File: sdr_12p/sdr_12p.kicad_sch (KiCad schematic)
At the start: 13 parts, among them J1 Rx, J10 ADAU1467_GPIOS, J11 ADAU1467_AUX_ADCS, J2 Tx, J3 6V, J4 2V, J5 4V, J6 Microcontroller, J7 USBi, J8 I2S2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

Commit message: changed project names
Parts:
- removed J4: 2V, symbol Connector:Screw_Terminal_01x02
- removed TR3, TR4: ADT4-6T, RF_Mini-Circuits:Mini-Circuits_CD637_H5.23mm, symbol Transformer:ADT4-6T
- added TR1, TR2: ADT1-1WT, RF_Mini-Circuits:Mini-Circuits_CD542_H2.84mm, symbol Transformer:ADT1-1WT

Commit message: basic arrangement of blocks
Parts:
- removed J5: 4V, symbol Connector:Screw_Terminal_01x02
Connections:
- net 6V renamed 6 - 20V
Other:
- sheet TRIPLE_ADAU1979 renamed TRIPLE_ADAU1978
- added sheet Coarse_VFO (coarse_vfo.kicad_sch)
- added sheet Microcontroller (microcontroller.kicad_sch)
- added sheet Power_Mgmt (power_mgmt.kicad_sch)
- sheet TRIPLE_ADAU1978: file triple_adau1979.kicad_sch -> triple_adau1978.kicad_sch
- title: HF Software Defined Radio with 32 Phase Polyphase Mixer -> HF Software Defined Radio with Polyphase Mixer (12 Phase)
- moved on the sheet: J10, J11, J3, J6, J7, J8, J9

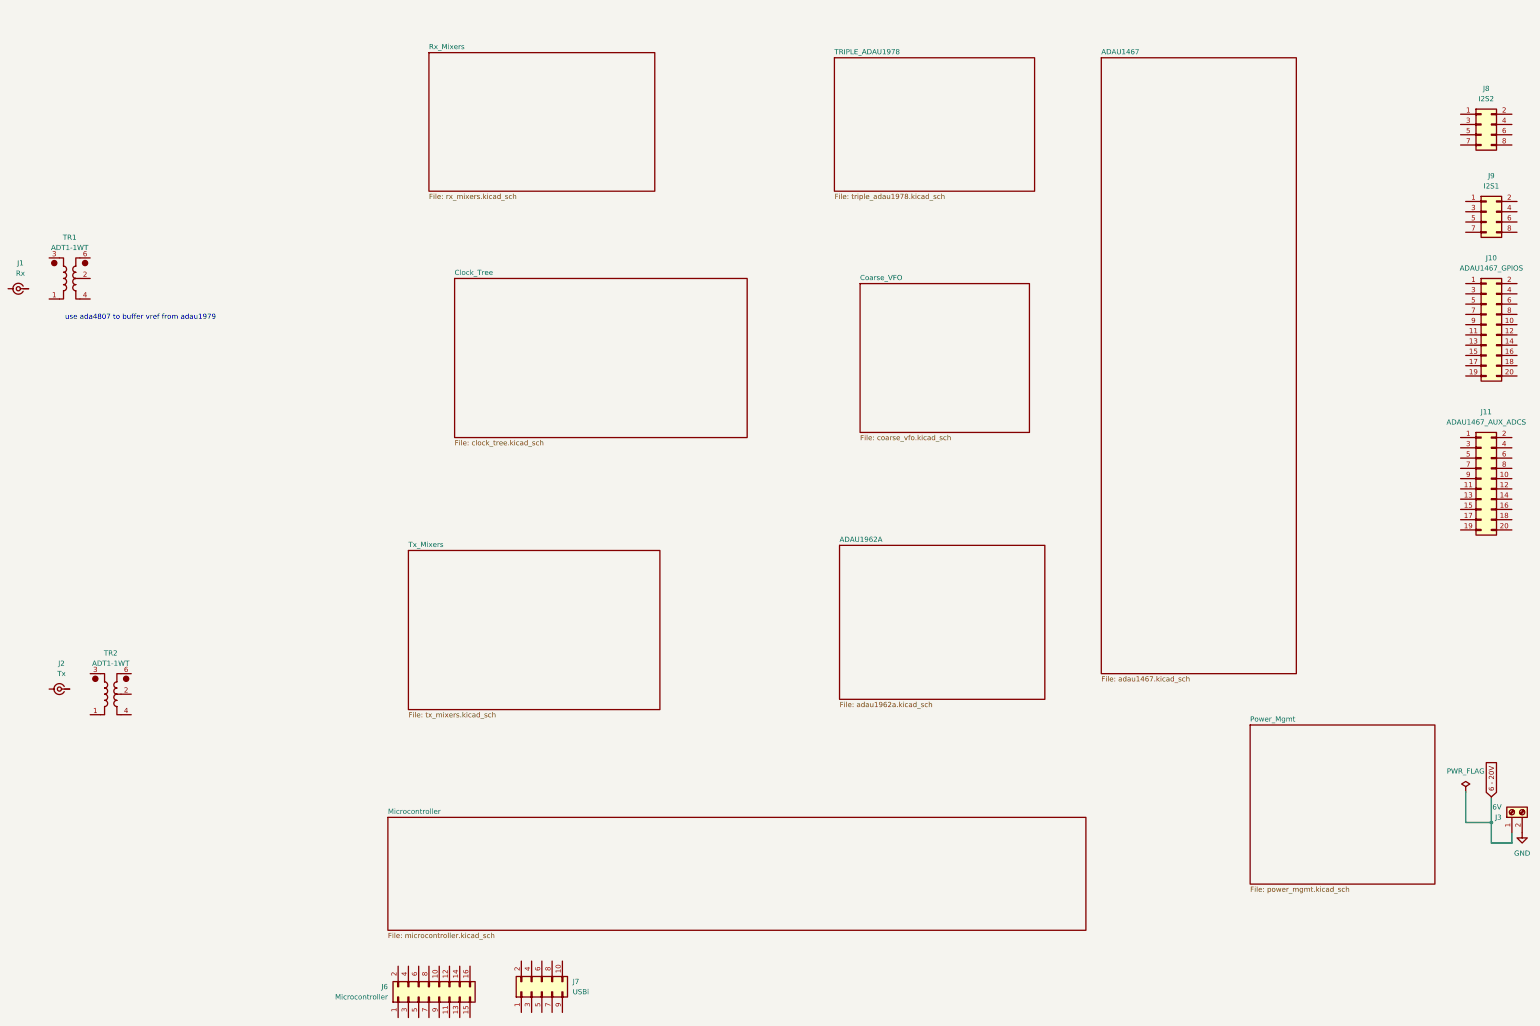
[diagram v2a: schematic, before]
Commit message: added rx switches
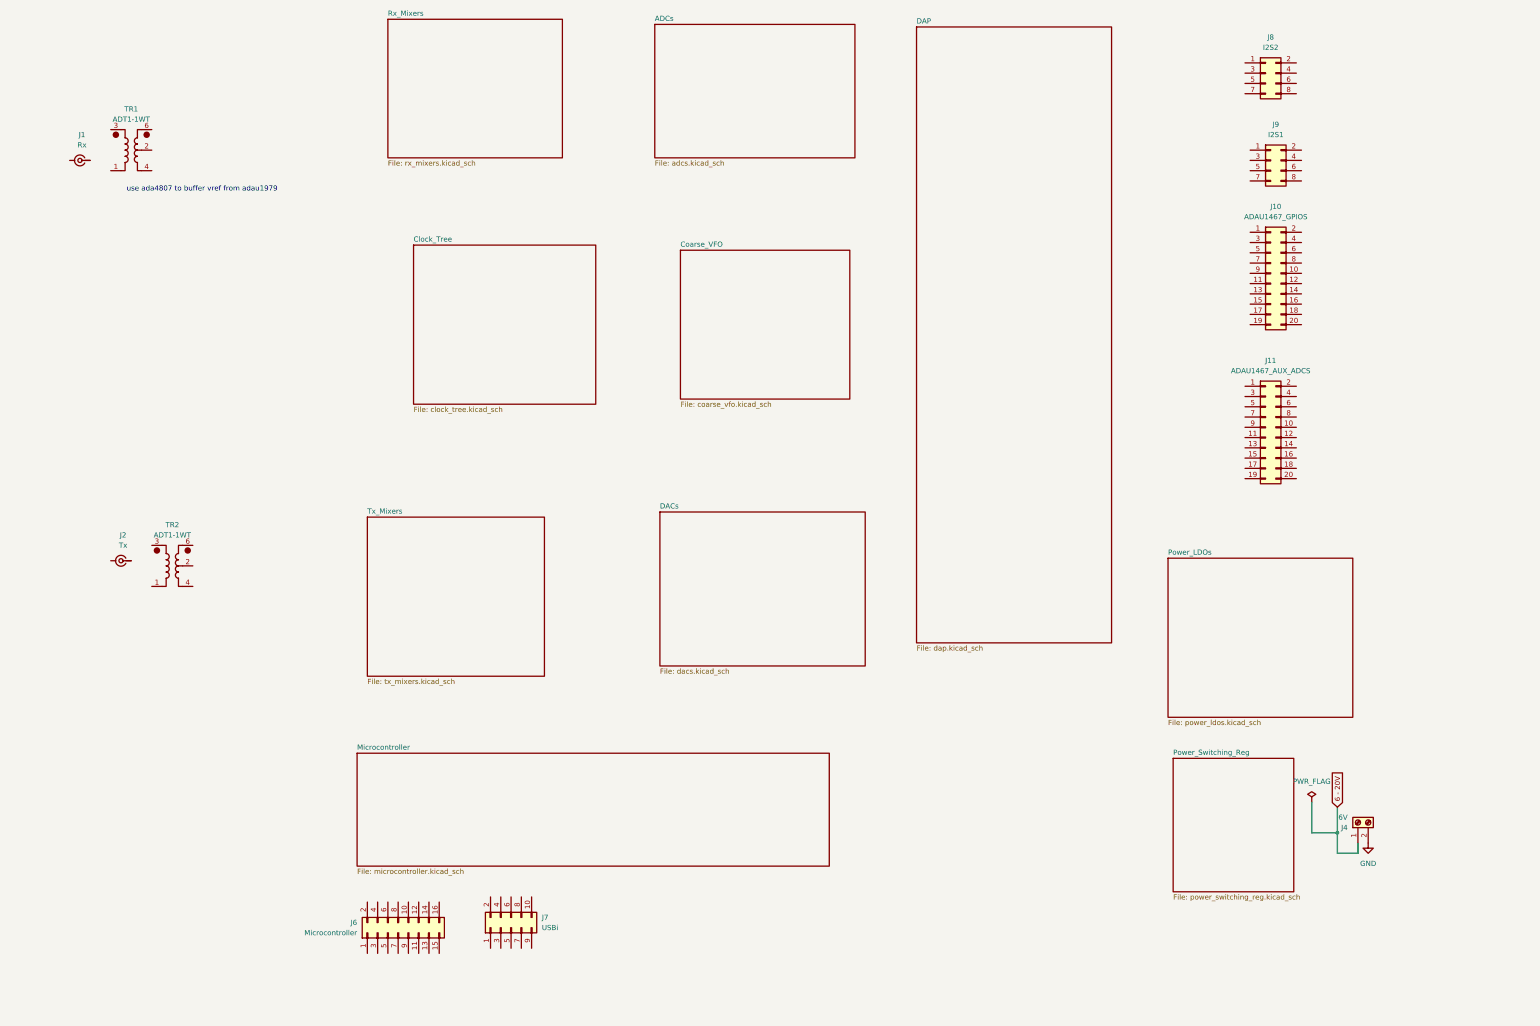
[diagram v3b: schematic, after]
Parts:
- removed J3: 6V, symbol Connector:Screw_Terminal_01x02
- added J4: 6V, symbol Connector:Screw_Terminal_01x02
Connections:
- net 6 - 20V: now also J4.1 (Pin_1)
- net GND: now also J4.2 (Pin_2)
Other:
- sheet ADAU1467 renamed DAP
- sheet ADAU1962A renamed DACs
- sheet Power_Mgmt renamed Power_LDOs
- sheet TRIPLE_ADAU1978 renamed ADCs
- added sheet Power_Switching_Reg (power_switching_reg.kicad_sch)
- sheet ADCs: file triple_adau1978.kicad_sch -> adcs.kicad_sch
- sheet DACs: file adau1962a.kicad_sch -> dacs.kicad_sch
- sheet DAP: file adau1467.kicad_sch -> dap.kicad_sch
- sheet Power_LDOs: file power_mgmt.kicad_sch -> power_ldos.kicad_sch
- moved on the sheet: J1, J10, J11, J2, J6, J7, J8, J9, TR1, TR2

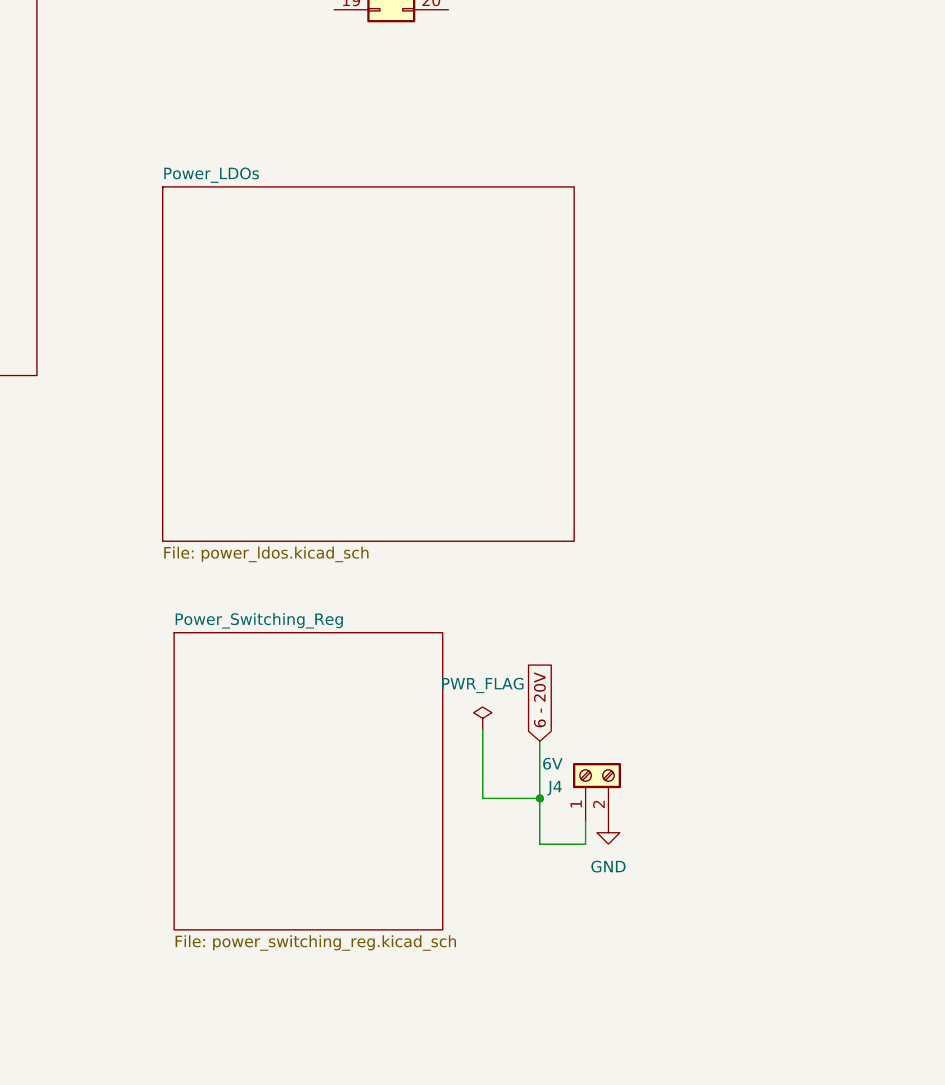
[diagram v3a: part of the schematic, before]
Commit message: added power mgmt
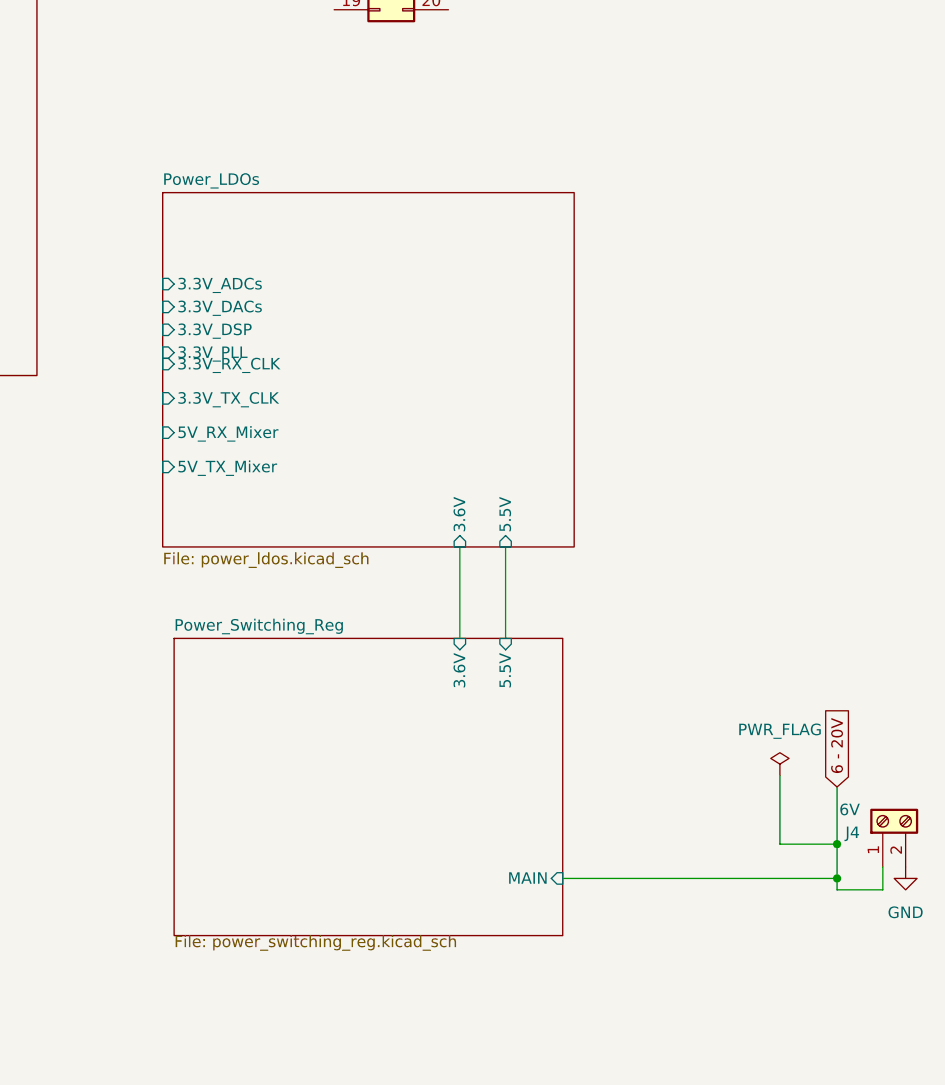
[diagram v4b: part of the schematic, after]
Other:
- sheet Power_LDOs ports: added 3.3V_ADCs, 3.3V_DACs, 3.3V_DSP, 3.3V_PLL, 3.3V_RX_CLK, 3.3V_TX_CLK, 3.6V, 5.5V, 5V_RX_Mixer, 5V_TX_Mixer; removed none
- sheet Power_Switching_Reg ports: added 3.6V, 5.5V, MAIN; removed none
- moved on the sheet: J4
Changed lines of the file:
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@@
 	)
 	(junction
-		(at 363.22 217.17)
+		(at 396.24 226.06)
 		(diameter 0)
 		(color 0 0 0 0)
 	)
+	(junction
+		(at 396.24 222.25)
+		(diameter 0)
+		(color 0 0 0 0)
+	)
 	(wire
 		(pts
-			(xy 368.3 222.25) (xy 363.22 222.25)
+			(xy 401.32 227.33) (xy 396.24 227.33)
 		)
 		(stroke
@@
 	(wire
 		(pts
-			(xy 363.22 217.17) (xy 363.22 222.25)
+			(xy 396.24 226.06) (xy 396.24 227.33)
 		)
 		(stroke
@@
 	(wire
 		(pts
-			(xy 368.3 219.71) (xy 368.3 222.25)
+			(xy 396.24 222.25) (xy 396.24 226.06)
 		)
 		(stroke
@@
 	(wire
 		(pts
-			(xy 356.87 209.55) (xy 356.87 217.17)
+			(xy 401.32 224.79) (xy 401.32 227.33)
 		)
 		(stroke
@@
 	(wire
 		(pts
-			(xy 356.87 217.17) (xy 363.22 217.17)
+			(xy 389.89 214.63) (xy 389.89 222.25)
 		)
 		(stroke
@@
 	(wire
 		(pts
-			(xy 363.22 210.82) (xy 363.22 217.17)
+			(xy 354.33 189.23) (xy 354.33 199.39)
 		)
 		(stroke
@@
 		)
 	)
+	(wire
+		(pts
+			(xy 365.76 226.06) (xy 396.24 226.06)
+		)
+		(stroke
+			(width 0)
+			(type default)
+		)
+	)
+	(wire
+		(pts
+			(xy 389.89 222.25) (xy 396.24 222.25)
+		)
+		(stroke
+			(width 0)
+			(type default)
+		)
+	)
+	(wire
+		(pts
+			(xy 396.24 215.9) (xy 396.24 222.25)
+		)
+		(stroke
+			(width 0)
+			(type default)
+		)
+	)
+	(wire
+		(pts
+			(xy 359.41 189.23) (xy 359.41 199.39)
+		)
+		(stroke
+			(width 0)
+			(type default)
+		)
+	)
 	(global_label "6 - 20V"
 		(shape input)
-		(at 363.22 210.82 90)
+		(at 396.24 215.9 90)
 		(fields_autoplaced yes)
 		(effects
@@
 		)
 		(property "Intersheetrefs" "${INTERSHEET_REFS}"
-			(at 363.22 199.6101 90)
+			(at 396.24 204.6901 90)
 			(effects
 				(font
@@
 	(symbol
 		(lib_id "Connector:Screw_Terminal_01x02")
-		(at 368.3 214.63 90)
+		(at 401.32 219.71 90)
 		(unit 1)
 		(exclude_from_sim no)
@@
 		(fields_autoplaced yes)
 		(property "Reference" "J4"
-			(at 365.76 215.9001 90)
+			(at 398.78 220.9801 90)
 			(effects
 				(font
@@
 		)
 		(property "Value" "6V"
-			(at 365.76 213.3601 90)
+			(at 398.78 218.4401 90)
 			(effects
 				(font
@@
 		)
 		(property "Footprint" ""
-			(at 368.3 214.63 0)
+			(at 401.32 219.71 0)
 			(effects
 				(font
@@
 		)
 		(property "Datasheet" "~"
-			(at 368.3 214.63 0)
+			(at 401.32 219.71 0)
 			(effects
 				(font
@@
 		)
 		(property "Description" "Generic screw terminal, single row, 01x02, script generated (kicad-library-utils/schlib/autogen/connector/)"
-			(at 368.3 214.63 0)
+			(at 401.32 219.71 0)
 			(effects
 				(font
@@
 	(symbol
 		(lib_id "power:GND")
-		(at 370.84 219.71 0)
+		(at 403.86 224.79 0)
 		(unit 1)
 		(exclude_from_sim no)
@@
 		(fields_autoplaced yes)
 		(property "Reference" "#PWR033"
-			(at 370.84 226.06 0)
+			(at 403.86 231.14 0)
 			(effects
 				(font
@@
 		)
 		(property "Value" "GND"
-			(at 370.84 224.79 0)
+			(at 403.86 229.87 0)
 			(effects
 				(font
@@
 		)
 		(property "Footprint" ""
-			(at 370.84 219.71 0)
+			(at 403.86 224.79 0)
 			(effects
 				(font
@@
 		)
 		(property "Datasheet" ""
-			(at 370.84 219.71 0)
+			(at 403.86 224.79 0)
 			(effects
 				(font
@@
 		)
 		(property "Description" "Power symbol creates a global label with name \"GND\" , ground"
-			(at 370.84 219.71 0)
+			(at 403.86 224.79 0)
 			(effects
 				(font
@@
 	(symbol
 		(lib_id "power:PWR_FLAG")
-		(at 356.87 209.55 0)
+		(at 389.89 214.63 0)
 		(unit 1)
 		(exclude_from_sim no)
@@
 		(fields_autoplaced yes)
 		(property "Reference" "#FLG01"
-			(at 356.87 207.645 0)
+			(at 389.89 212.725 0)
 			(effects
 				(font
@@
 		)
 		(property "Value" "PWR_FLAG"
-			(at 356.87 204.47 0)
+			(at 389.89 209.55 0)
 			(effects
 				(font
@@
 		)
 		(property "Footprint" ""
-			(at 356.87 209.55 0)
+			(at 389.89 214.63 0)
 			(effects
 				(font
@@
 		)
 		(property "Datasheet" "~"
-			(at 356.87 209.55 0)
+			(at 389.89 214.63 0)
 			(effects
 				(font
@@
 		)
 		(property "Description" "Special symbol for telling ERC where power comes from"
-			(at 356.87 209.55 0)
+			(at 389.89 214.63 0)
 			(effects
 				(font
@@
 	)
 	(sheet
-		(at 322.58 198.755)
-		(size 29.845 33.02)
+		(at 322.58 199.39)
+		(size 43.18 33.02)
 		(exclude_from_sim no)
 		(in_bom yes)
@@
 		)
 		(property "Sheetname" "Power_Switching_Reg"
-			(at 322.58 198.0434 0)
+			(at 322.58 198.6784 0)
 			(effects
 				(font
@@
 				)
 				(justify left top)
+			)
+		)
+		(pin "MAIN" input
+			(at 365.76 226.06 0)
+			(effects
+				(font
+					(size 1.27 1.27)
+				)
+				(justify right)
+			)
+		)
+		(pin "3.6V" input
+			(at 354.33 199.39 90)
+			(effects
+				(font
+					(size 1.27 1.27)
+				)
+				(justify right)
+			)
+		)
+		(pin "5.5V" input
+			(at 359.41 199.39 90)
+			(effects
+				(font
+					(size 1.27 1.27)
+				)
+				(justify right)
 			)
 		)
@@
 	)
 	(sheet
-		(at 321.31 149.225)
+		(at 321.31 149.86)
 		(size 45.72 39.37)
 		(exclude_from_sim no)
@@
 		)
 		(property "Sheetname" "Power_LDOs"
-			(at 321.31 148.5134 0)
+			(at 321.31 149.1484 0)
 			(effects
 				(font
@@
 		)
 		(property "Sheetfile" "power_ldos.kicad_sch"
-			(at 321.31 189.1796 0)
+			(at 321.31 189.8146 0)
 			(effects
 				(font
@@
 			)
 		)
+		(pin "5V_TX_Mixer" input
+			(at 321.31 180.34 180)
+			(effects
+				(font
+					(size 1.27 1.27)
+				)
+				(justify left)
+			)
+		)
+		(pin "5.5V" input
+			(at 359.41 189.23 270)
+			(effects
+				(font
+					(size 1.27 1.27)
+				)
+				(justify left)
+			)
+		)
+		(pin "3.6V" input
+			(at 354.33 189.23 270)
+			(effects
+				(font
+					(size 1.27 1.27)
+				)
+				(justify left)
+			)
+		)
+		(pin "3.3V_ADCs" input
+			(at 321.31 160.02 180)
+			(effects
+				(font
+					(size 1.27 1.27)
+				)
+				(justify left)
+			)
+		)
+		(pin "3.3V_DACs" input
+			(at 321.31 162.56 180)
+			(effects
+				(font
+					(size 1.27 1.27)
+				)
+				(justify left)
+			)
+		)
+		(pin "3.3V_DSP" input
+			(at 321.31 165.1 180)
+			(effects
+				(font
+					(size 1.27 1.27)
+				)
+				(justify left)
+			)
+		)
+		(pin "3.3V_PLL" input
+			(at 321.31 167.64 180)
+			(effects
+				(font
+					(size 1.27 1.27)
+				)
+				(justify left)
+			)
+		)
+		(pin "3.3V_RX_CLK" input
+			(at 321.31 168.91 180)
+			(effects
+				(font
+					(size 1.27 1.27)
+				)
+				(justify left)
+			)
+		)
+		(pin "3.3V_TX_CLK" input
+			(at 321.31 172.72 180)
+			(effects
+				(font
+					(size 1.27 1.27)
+				)
+				(justify left)
+			)
+		)
+		(pin "5V_RX_Mixer" input
+			(at 321.31 176.53 180)
+			(effects
+				(font
+					(size 1.27 1.27)
+				)
+				(justify left)
+			)
+		)
